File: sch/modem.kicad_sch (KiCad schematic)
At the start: 35 parts, among them J10 20579-001E, J11 20579-001E, J12 20579-001E, J13 20579-001E, J14 732511150, J15 732511150, J16 732511150, J17 732511150, J9 M.2_Socket_B, P1 SF72S006VBDR2500, Q3 NX3008NBKW_115, T1 TestPoint, T2 TestPoint, T3 TestPoint, T4 TestPoint, T5 TestPoint, U9 ESD7004MUTAG

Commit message: Fjernet gammelt og la til nye komponenter, merging ferdig
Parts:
- renumbered C37 to C5, C38 to C?, C41 to C?, C39 to C?, C40 to C?, C42 to C?, U9 to CR3, D4 to D1, D3 to D?, J10 to J?, J14 to J?, J12 to J?, J15 to J?, J11 to J?, J16 to J?, J17 to J?, J13 to J?, MP5 to MP?, MP6 to MP?, R21 to R?, R16 to R?, R22 to R?, R18 to R?, R17 to R?, R20 to R?, R15 to R?, R19 to R?, T1 to TP1, T2 to TP2, T3 to TP3, T4 to TP4, T5 to TP5

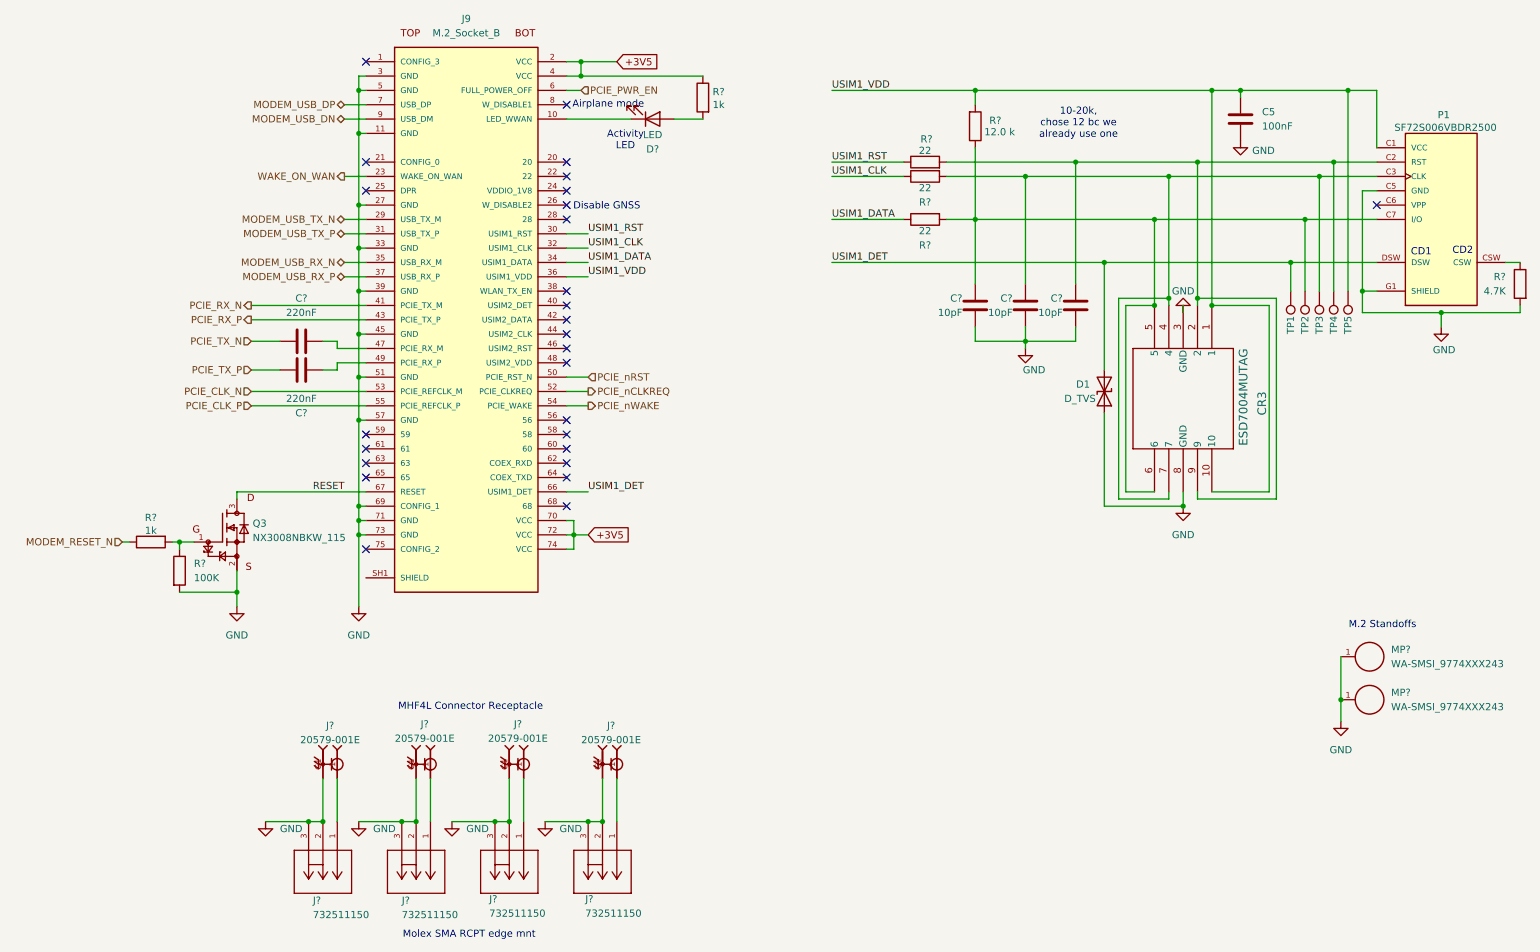
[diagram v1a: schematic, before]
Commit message: Ferdig pcb-layout modem og simkort, ikke kobla til CM enda
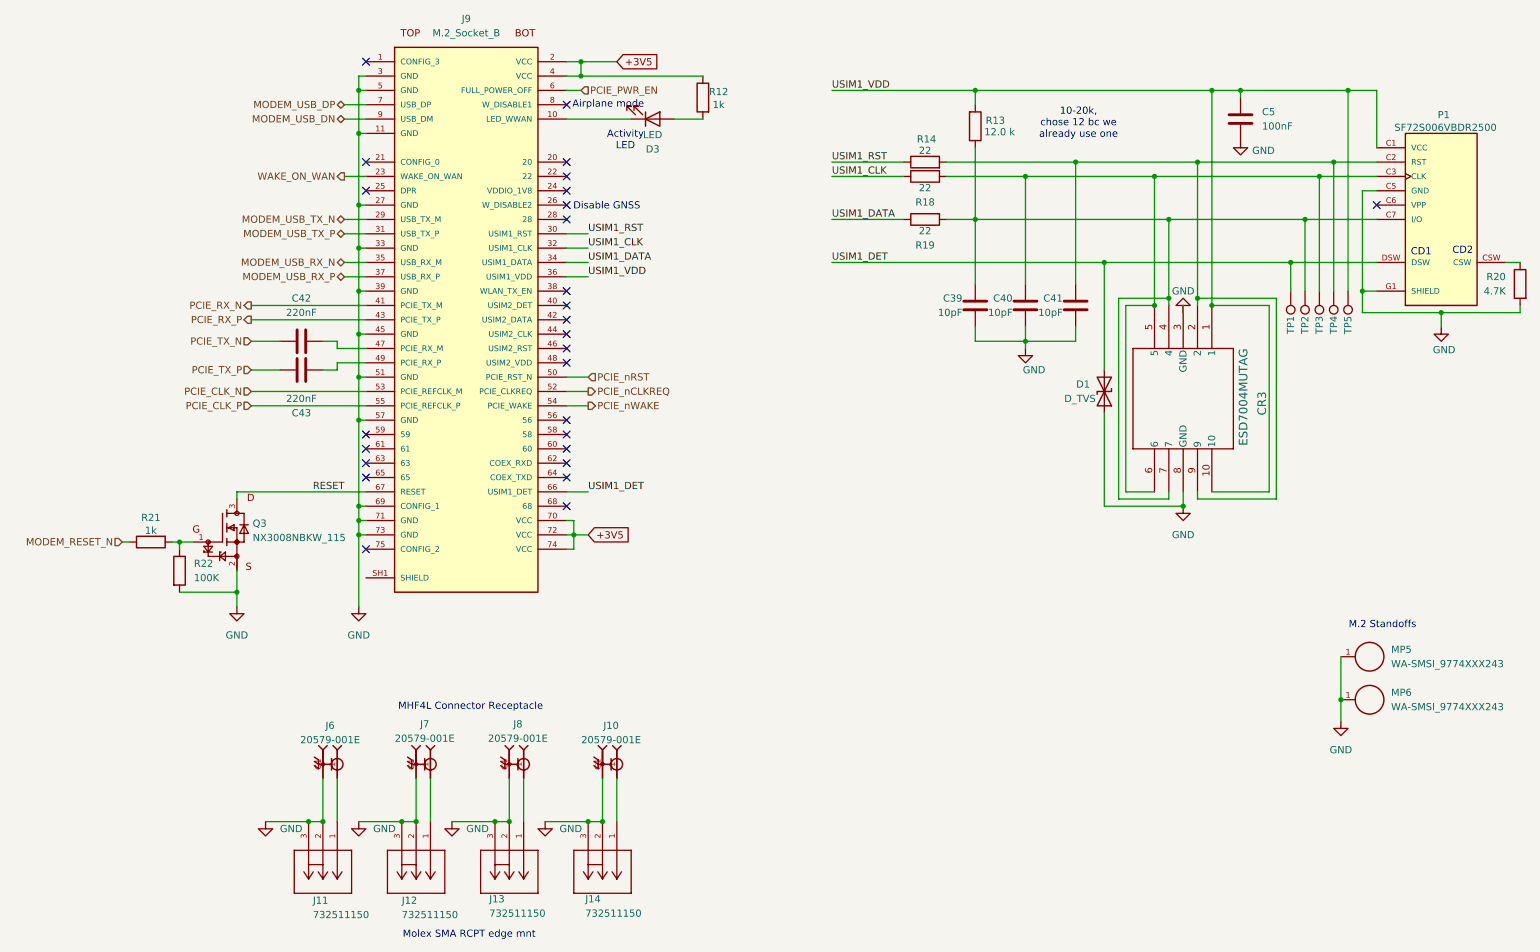
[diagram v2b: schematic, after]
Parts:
- gave numbers to parts that had none: 24
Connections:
- net at C40.1, P1.C3 (CLK), R18.2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: now also CR3.5, CR3.6; no longer CR3.4, CR3.7
- net at C39.1, P1.C7 (I/O), R13.1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: now also CR3.4, CR3.7; no longer CR3.5, CR3.6

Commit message: Routa SD-lytte på cm på nytt
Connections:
- net at C40.1, P1.C3 (CLK), R18.2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: no longer CR3.5, CR3.6
- new net: CR3.5, CR3.6
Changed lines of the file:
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@@
-	)
-	(junction
-		(at 213.36 48.26)
-		(diameter 0)
-		(color 0 0 0 0)
 	)
 	(junction
@@
 	)
 	(junction
-		(at 213.36 71.12)
-		(diameter 0)
-		(color 0 0 0 0)
-	)
-	(junction
 		(at 72.39 111.76)
 		(diameter 0)
@@
 	(wire
 		(pts
-			(xy 213.36 48.26) (xy 242.57 48.26)
-		)
-		(stroke
-			(width 0)
-			(type default)
-		)
-	)
-	(wire
-		(pts
 			(xy 237.49 63.5) (xy 252.73 63.5)
 		)
@@
 	(wire
 		(pts
-			(xy 190.5 48.26) (xy 213.36 48.26)
+			(xy 190.5 48.26) (xy 242.57 48.26)
 		)
 		(stroke
@@
 		)
 		(stroke
-			(width 0)
-			(type default)
-		)
-	)
-	(wire
-		(pts
-			(xy 213.36 48.26) (xy 213.36 71.12)
-		)
-		(stroke

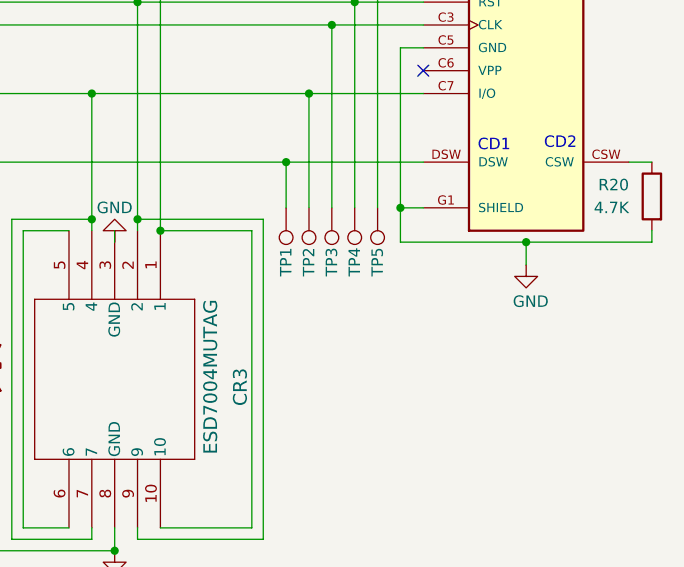
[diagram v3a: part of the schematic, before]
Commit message: added libs for footprints
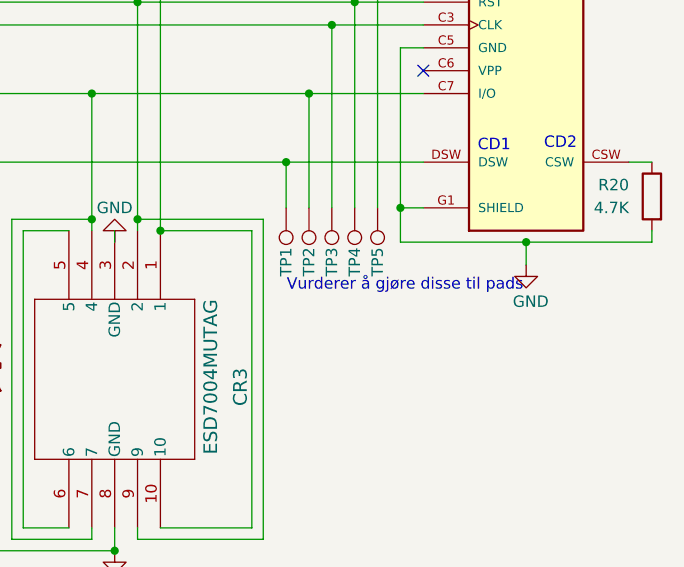
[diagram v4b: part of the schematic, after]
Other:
- note added: "Vurderer å gjøre disse til pads"
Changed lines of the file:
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@@
+		)
+	)
+	(text "Vurderer å gjøre disse til pads"
+		(exclude_from_sim no)
+		(at 250.698 77.216 0)
+		(effects
+			(font
+				(size 1.27 1.27)
+			)
 		)
 	)

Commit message: bytta ut TP-loops med pads, begynt modem-cm layout
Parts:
- TP1, TP2, TP3, TP4, TP5: footprint TestPoint:TestPoint_Loop_D2.60mm_Drill1.6mm_Beaded -> TestPoint:TestPoint_Pad_D1.0mm
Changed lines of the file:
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@@
 			)
 		)
-		(property "Footprint" "TestPoint:TestPoint_Loop_D2.60mm_Drill1.6mm_Beaded"
+		(property "Footprint" "TestPoint:TestPoint_Pad_D1.0mm"
 			(at 232.41 68.58 0)
 			(effects
@@
 	)
 	(symbol
-		(lib_id "Connector:TestPoint")
-		(at 245.11 68.58 180)
-		(unit 1)
-		(exclude_from_sim no)
-		(in_bom yes)
-		(on_board yes)
-		(dnp no)
-		(property "Reference" "TP4"
-			(at 245.11 76.2 90)
-			(effects
-				(font
-					(size 1.27 1.27)
-				)
-				(justify right)
-			)
-		)
-		(property "Value" "TestPoint"
-			(at 242.57 70.6121 0)
-			(effects
-				(font
-					(size 1.27 1.27)
-				)
-				(justify left)
-				(hide yes)
-			)
-		)
-		(property "Footprint" "TestPoint:TestPoint_Loop_D2.60mm_Drill1.6mm_Beaded"
-			(at 240.03 68.58 0)
-			(effects
-				(font
-					(size 1.27 1.27)
-				)
-				(hide yes)
-			)
-		)
-		(property "Datasheet" "~"
-			(at 240.03 68.58 0)
-			(effects
-				(font
-					(size 1.27 1.27)
-				)
-				(hide yes)
-			)
-		)
-		(property "Description" "test point"
-			(at 245.11 68.58 0)
-			(effects
-				(font
-					(size 1.27 1.27)
-				)
-				(hide yes)
-			)
-		)
-		(pin "1"
-		)
-		(instances
-			(project "audiograb"
-				(path "/c46c2311-6d4b-411d-b012-c7730eac136d/0ab7621d-5895-4cff-b488-abb2b98a38d3"
-					(reference "TP4")
-					(unit 1)
-				)
-			)
-		)
-	)
-	(symbol
 		(lib_id "WA-SMSI_9774XXX243:WA-SMSI_9774XXX243")
 		(at 251.46 133.35 0)
@@
 	)
 	(symbol
+		(lib_id "Connector:TestPoint")
+		(at 245.11 68.58 180)
+		(unit 1)
+		(exclude_from_sim no)
+		(in_bom yes)
+		(on_board yes)
+		(dnp no)
+		(property "Reference" "TP4"
+			(at 245.11 76.2 90)
+			(effects
+				(font
+					(size 1.27 1.27)
+				)
+				(justify right)
+			)
+		)
+		(property "Value" "TestPoint"
+			(at 242.57 70.6121 0)
+			(effects
+				(font
+					(size 1.27 1.27)
+				)
+				(justify left)
+				(hide yes)
+			)
+		)
+		(property "Footprint" "TestPoint:TestPoint_Pad_D1.0mm"
+			(at 240.03 68.58 0)
+			(effects
+				(font
+					(size 1.27 1.27)
+				)
+				(hide yes)
+			)
+		)
+		(property "Datasheet" "~"
+			(at 240.03 68.58 0)
+			(effects
+				(font
+					(size 1.27 1.27)
+				)
+				(hide yes)
+			)
+		)
+		(property "Description" "test point"
+			(at 245.11 68.58 0)
+			(effects
+				(font
+					(size 1.27 1.27)
+				)
+				(hide yes)
+			)
+		)
+		(pin "1"
+		)
+		(instances
+			(project "audiograb"
+				(path "/c46c2311-6d4b-411d-b012-c7730eac136d/0ab7621d-5895-4cff-b488-abb2b98a38d3"
+					(reference "TP4")
+					(unit 1)
+				)
+			)
+		)
+	)
+	(symbol
 		(lib_id "732511150:732511150")
 		(at 85.09 162.56 270)
@@
 			)
 		)
-		(property "Footprint" "TestPoint:TestPoint_Loop_D2.60mm_Drill1.6mm_Beaded"
+		(property "Footprint" "TestPoint:TestPoint_Pad_D1.0mm"
 			(at 234.95 68.58 0)
 			(effects
@@
 	)
 	(symbol
+		(lib_id "Connector:TestPoint")
+		(at 247.65 68.58 180)
+		(unit 1)
+		(exclude_from_sim no)
+		(in_bom yes)
+		(on_board yes)
+		(dnp no)
+		(property "Reference" "TP5"
+			(at 247.65 76.2 90)
+			(effects
+				(font
+					(size 1.27 1.27)
+				)
+				(justify right)
+			)
+		)
+		(property "Value" "TestPoint"
+			(at 245.11 70.6121 0)
+			(effects
+				(font
+					(size 1.27 1.27)
+				)
+				(justify left)
+				(hide yes)
+			)
+		)
+		(property "Footprint" "TestPoint:TestPoint_Pad_D1.0mm"
+			(at 242.57 68.58 0)
+			(effects
+				(font
+					(size 1.27 1.27)
+				)
+				(hide yes)
+			)
+		)
+		(property "Datasheet" "~"
+			(at 242.57 68.58 0)
+			(effects
+				(font
+					(size 1.27 1.27)
+				)
+				(hide yes)
+			)
+		)
+		(property "Description" "test point"
+			(at 247.65 68.58 0)
+			(effects
+				(font
+					(size 1.27 1.27)
+				)
+				(hide yes)
+			)
+		)
+		(pin "1"
+		)
+		(instances
+			(project "audiograb"
+				(path "/c46c2311-6d4b-411d-b012-c7730eac136d/0ab7621d-5895-4cff-b488-abb2b98a38d3"
+					(reference "TP5")
+					(unit 1)
+				)
+			)
+		)
+	)
+	(symbol
 		(lib_id "power:GND")
 		(at 88.9 162.56 0)
@@
 	)
 	(symbol
+		(lib_id "Connector:TestPoint")
+		(at 242.57 68.58 180)
+		(unit 1)
+		(exclude_from_sim no)
+		(in_bom yes)
+		(on_board yes)
+		(dnp no)
+		(property "Reference" "TP3"
+			(at 242.57 76.2 90)
+			(effects
+				(font
+					(size 1.27 1.27)
+				)
+				(justify right)
+			)
+		)
+		(property "Value" "TestPoint"
+			(at 240.03 70.6121 0)
+			(effects
+				(font
+					(size 1.27 1.27)
+				)
+				(justify left)
+				(hide yes)
+			)
+		)
+		(property "Footprint" "TestPoint:TestPoint_Pad_D1.0mm"
+			(at 237.49 68.58 0)
+			(effects
+				(font
+					(size 1.27 1.27)
+				)
+				(hide yes)
+			)
+		)
+		(property "Datasheet" "~"
+			(at 237.49 68.58 0)
+			(effects
+				(font
+					(size 1.27 1.27)
+				)
+				(hide yes)
+			)
+		)
+		(property "Description" "test point"
+			(at 242.57 68.58 0)
+			(effects
+				(font
+					(size 1.27 1.27)
+				)
+				(hide yes)
+			)
+		)
+		(pin "1"
+		)
+		(instances
+			(project "audiograb"
+				(path "/c46c2311-6d4b-411d-b012-c7730eac136d/0ab7621d-5895-4cff-b488-abb2b98a38d3"
+					(reference "TP3")
+					(unit 1)
+				)
+			)
+		)
+	)
+	(symbol
 		(lib_id "Device:C")
 		(at 62.23 82.55 90)
@@
 	)
 	(symbol
-		(lib_id "Connector:TestPoint")
-		(at 247.65 68.58 180)
-		(unit 1)
-		(exclude_from_sim no)
-		(in_bom yes)
-		(on_board yes)
-		(dnp no)
-		(property "Reference" "TP5"
-			(at 247.65 76.2 90)
-			(effects
-				(font
-					(size 1.27 1.27)
-				)
-				(justify right)
-			)
-		)
-		(property "Value" "TestPoint"
-			(at 245.11 70.6121 0)
-			(effects
-				(font
-					(size 1.27 1.27)
-				)
-				(justify left)
-				(hide yes)
-			)
-		)
-		(property "Footprint" "TestPoint:TestPoint_Loop_D2.60mm_Drill1.6mm_Beaded"
-			(at 242.57 68.58 0)
-			(effects
-				(font
-					(size 1.27 1.27)
-				)
-				(hide yes)
-			)
-		)
-		(property "Datasheet" "~"
-			(at 242.57 68.58 0)
-			(effects
-				(font
-					(size 1.27 1.27)
-				)
-				(hide yes)
-			)
-		)
-		(property "Description" "test point"
-			(at 247.65 68.58 0)
-			(effects
-				(font
-					(size 1.27 1.27)
-				)
-				(hide yes)
-			)
-		)
-		(pin "1"
-		)
-		(instances
-			(project "audiograb"
-				(path "/c46c2311-6d4b-411d-b012-c7730eac136d/0ab7621d-5895-4cff-b488-abb2b98a38d3"
-					(reference "TP5")
-					(unit 1)
-				)
-			)
-		)
-	)
-	(symbol
 		(lib_id "Device:R")
 		(at 172.72 48.26 90)
@@
 					(unit 1)
 				)
-			)
-		)
-	)
-	(symbol
-		(lib_id "Connector:TestPoint")
-		(at 242.57 68.58 180)
-		(unit 1)
-		(exclude_from_sim no)
-		(in_bom yes)
-		(on_board yes)
-		(dnp no)
-		(property "Reference" "TP3"
-			(at 242.57 76.2 90)
-			(effects
-				(font
-					(size 1.27 1.27)
-				)
-				(justify right)
-			)
-		)
-		(property "Value" "TestPoint"
-			(at 240.03 70.6121 0)
-			(effects
-				(font
-					(size 1.27 1.27)
-				)
-				(justify left)
-				(hide yes)
-			)
-		)
-		(property "Footprint" "TestPoint:TestPoint_Loop_D2.60mm_Drill1.6mm_Beaded"
-			(at 237.49 68.58 0)
-			(effects
-				(font
-					(size 1.27 1.27)
-				)
-				(hide yes)
-			)
-		)
-		(property "Datasheet" "~"
-			(at 237.49 68.58 0)
-			(effects
-				(font
-					(size 1.27 1.27)
-				)
-				(hide yes)
-			)
-		)
-		(property "Description" "test point"
-			(at 242.57 68.58 0)
-			(effects
-				(font
-					(size 1.27 1.27)
-				)
-				(hide yes)
-			)
-		)
-		(pin "1"
-		)
-		(instances
-			(project "audiograb"
-				(path "/c46c2311-6d4b-411d-b012-c7730eac136d/0ab7621d-5895-4cff-b488-abb2b98a38d3"
-					(reference "TP3")
-					(unit 1)
-				)

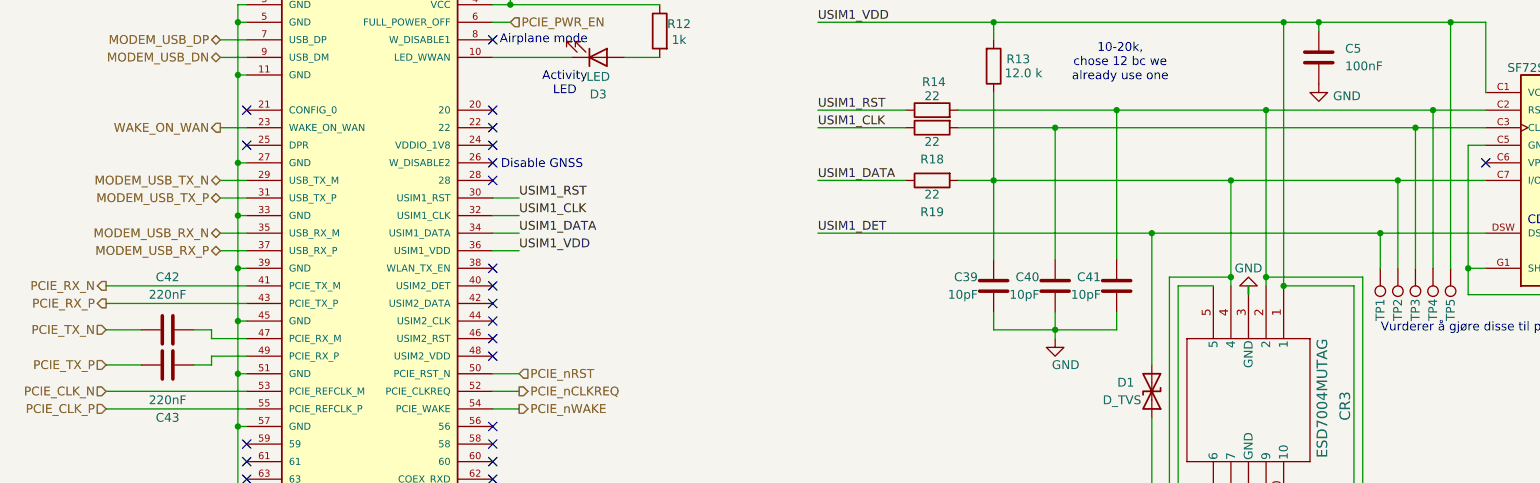
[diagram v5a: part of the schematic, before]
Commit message: Fiksa all routing CM-Modem-SIM-GPIO++, mangle fill og rule zones
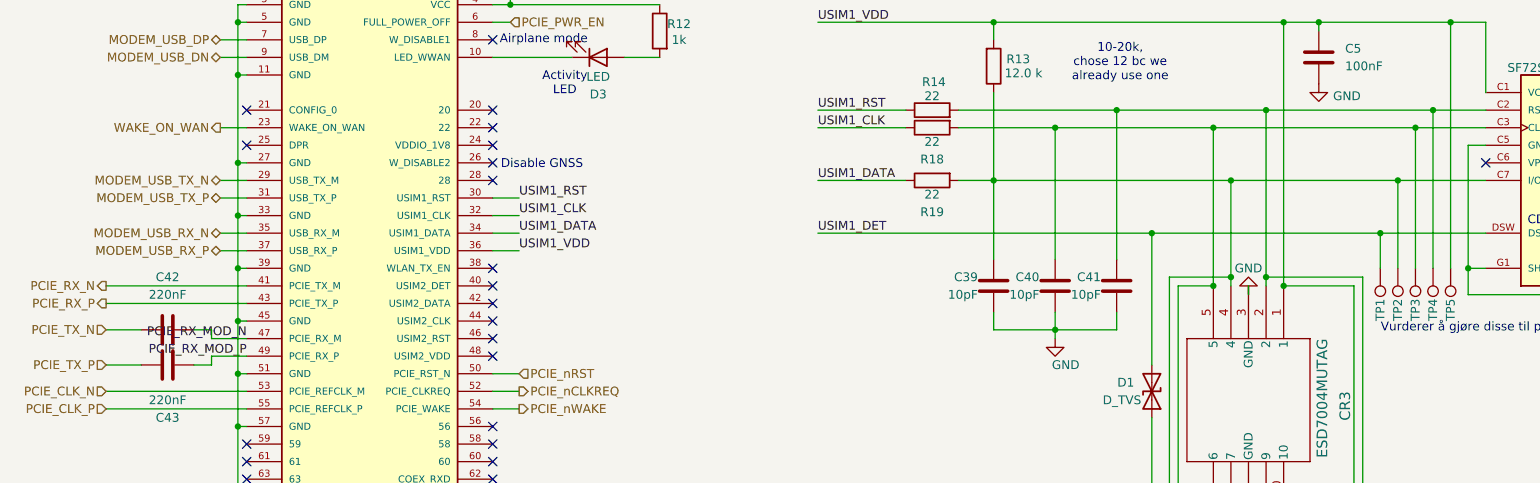
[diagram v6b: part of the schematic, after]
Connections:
- net at C40.1, P1.C3 (CLK), R18.2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: now also CR3.5, CR3.6
- net PCIE_RX_MOD_N: now reaches C42.2, J9.47 (PCIE_RX_M)
- net PCIE_RX_MOD_P: now reaches C43.2, J9.49 (PCIE_RX_P)
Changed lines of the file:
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@@
+	)
+	(junction
+		(at 213.36 71.12)
+		(diameter 0)
+		(color 0 0 0 0)
+	)
+	(junction
+		(at 213.36 48.26)
+		(diameter 0)
+		(color 0 0 0 0)
 	)
 	(junction
@@
 	(wire
 		(pts
-			(xy 190.5 48.26) (xy 242.57 48.26)
+			(xy 190.5 48.26) (xy 213.36 48.26)
 		)
 		(stroke
@@
 	(wire
 		(pts
+			(xy 213.36 48.26) (xy 213.36 71.12)
+		)
+		(stroke
+			(width 0)
+			(type default)
+		)
+	)
+	(wire
+		(pts
 			(xy 240.03 55.88) (xy 252.73 55.88)
 		)
@@
 		(pts
 			(xy 73.66 81.28) (xy 68.58 81.28)
+		)
+		(stroke
+			(width 0)
+			(type default)
+		)
+	)
+	(wire
+		(pts
+			(xy 213.36 48.26) (xy 242.57 48.26)
 		)
 		(stroke
@@
 		)
 	)
+	(label "PCIE_RX_MOD_P"
+		(at 73.66 81.28 180)
+		(effects
+			(font
+				(size 1.27 1.27)
+			)
+			(justify right bottom)
+		)
+	)
 	(label "USIM1_DET"
 		(at 113.03 104.14 0)
@@
 		)
 	)
+	(label "PCIE_RX_MOD_N"
+		(at 73.66 78.74 180)
+		(effects
+			(font
+				(size 1.27 1.27)
+			)
+			(justify right bottom)
+		)
+	)
